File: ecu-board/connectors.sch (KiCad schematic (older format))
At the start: 39 parts, among them J10 Injector connector, J11 Cockpit connector, J12 EGO connector, J13 Chrankshaft Hall connector, J14 Camshaft Hall connector, J15 Ignition 1 connector, J16 Ignition 2 connector, J17 Camera connector, J18 Wheel Hall connector, J19 Speed sensor connector, J2 Battery power conenctor, J20 CAN connector, J21 12V connector, J22 PWRGND connector, J4 Motor connector, J5 Serial DB9 connector, J6 Controller connector, J7 Backlight connector, J8 IAT connector, J9 CLT connector

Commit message: Correct BOM to present components.
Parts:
- D10, D6, D7, D8, D9: Manufacturer (none) -> Generic; Part no. 3mm T-1 -> 0805
- D11: Manufacturer (none) -> ON Semi; Part no. (none) -> 1N5820G
- JP2, JP3, R10, R11, R5, R6, R7, R8, R9: Manufacturer (none) -> Generic; Part no. (none) -> 0805
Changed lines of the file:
@@
 F 1 "Ignition 1 connector" H 7330 3301 50  0000 L CNN
 F 2 "ecu-board-footprints:Terminal_Block_3x5.00mm" H 7250 3350 50  0001 C CNN
-F 3 "http://www.farnell.com/datasheets/2308387.pdf?_ga=2.20224184.1892952727.1549112209-881392492.1520553087" H 7250 3350 50  0001 C CNN
+F 3 "~" H 7250 3350 50  0001 C CNN
 F 4 "Würth" H 7250 3350 50  0001 C CNN "Manufacturer"
 F 5 "2141 Series" H 7250 3350 50  0001 C CNN "Part no."
@@
 F 1 "Ignition 2 connector" H 7330 4101 50  0000 L CNN
 F 2 "ecu-board-footprints:Terminal_Block_3x5.00mm" H 7250 4150 50  0001 C CNN
-F 3 "http://www.farnell.com/datasheets/2308387.pdf?_ga=2.20224184.1892952727.1549112209-881392492.1520553087" H 7250 4150 50  0001 C CNN
+F 3 "~" H 7250 4150 50  0001 C CNN
 F 4 "Würth" H 7250 4150 50  0001 C CNN "Manufacturer"
 F 5 "2141 Series" H 7250 4150 50  0001 C CNN "Part no."
@@
 F 2 "Resistors_SMD:R_0805_HandSoldering" V 9180 2000 50  0001 C CNN
 F 3 "~" H 9250 2000 50  0001 C CNN
+F 4 "Generic" H 9250 2000 50  0001 C CNN "Manufacturer"
+F 5 "0805" H 9250 2000 50  0001 C CNN "Part no."
 	1    9250 2000
 	1    0    0    -1
@@
 F 2 "Resistors_SMD:R_0805_HandSoldering" H 9250 3150 50  0001 C CNN
 F 3 "~" H 9250 3150 50  0001 C CNN
+F 4 "Generic" H 9250 3150 50  0001 C CNN "Manufacturer"
+F 5 "0805" H 9250 3150 50  0001 C CNN "Part no."
 	1    9250 3150
 	0    -1   -1   0
@@
 F 2 "Resistors_SMD:R_0805_HandSoldering" H 9250 4300 50  0001 C CNN
 F 3 "~" H 9250 4300 50  0001 C CNN
+F 4 "Generic" H 9250 4300 50  0001 C CNN "Manufacturer"
+F 5 "0805" H 9250 4300 50  0001 C CNN "Part no."
 	1    9250 4300
 	0    -1   -1   0
@@
 F 1 "LED" H 1442 2914 50  0000 C CNN
 F 2 "LEDs:LED_0805_HandSoldering" H 1450 2700 50  0001 C CNN
-F 3 "" H 1450 2700 50  0001 C CNN
-F 4 "3mm T-1" H 1450 2700 50  0001 C CNN "Part no."
+F 3 "~" H 1450 2700 50  0001 C CNN
+F 4 "0805" H 1450 2700 50  0001 C CNN "Part no."
+F 5 "Generic" H 1450 2700 50  0001 C CNN "Manufacturer"
 	1    1450 2700
 	-1   0    0    1
@@
 F 2 "LEDs:LED_0805_HandSoldering" H 1850 4450 50  0001 C CNN
 F 3 "~" H 1850 4450 50  0001 C CNN
-F 4 "3mm T-1" H 1850 4450 50  0001 C CNN "Part no."
+F 4 "0805" H 1850 4450 50  0001 C CNN "Part no."
+F 5 "Generic" H 1850 4450 50  0001 C CNN "Manufacturer"
 	1    1850 4450
 	-1   0    0    1
@@
 F 2 "LEDs:LED_0805_HandSoldering" H 7400 1500 50  0001 C CNN
 F 3 "~" H 7400 1500 50  0001 C CNN
-F 4 "3mm T-1" H 7400 1500 50  0001 C CNN "Part no."
+F 4 "0805" H 7400 1500 50  0001 C CNN "Part no."
+F 5 "Generic" H 7400 1500 50  0001 C CNN "Manufacturer"
 	1    7400 1500
 	-1   0    0    1
@@
 F 2 "LEDs:LED_0805_HandSoldering" H 2550 7600 50  0001 C CNN
 F 3 "~" H 2550 7600 50  0001 C CNN
-F 4 "3mm T-1" H 2550 7600 50  0001 C CNN "Part no."
+F 4 "0805" H 2550 7600 50  0001 C CNN "Part no."
+F 5 "Generic" H 2550 7600 50  0001 C CNN "Manufacturer"
 	1    2550 7600
 	-1   0    0    1
@@
 F 2 "Resistors_SMD:R_0805_HandSoldering" V 1030 2700 50  0001 C CNN
 F 3 "~" H 1100 2700 50  0001 C CNN
+F 4 "Generic" H 1100 2700 50  0001 C CNN "Manufacturer"
+F 5 "0805" H 1100 2700 50  0001 C CNN "Part no."
 	1    1100 2700
 	0    1    -1   0
@@
 F 2 "Resistors_SMD:R_0805_HandSoldering" V 1430 4450 50  0001 C CNN
 F 3 "~" H 1500 4450 50  0001 C CNN
+F 4 "Generic" H 1500 4450 50  0001 C CNN "Manufacturer"
+F 5 "0805" H 1500 4450 50  0001 C CNN "Part no."
 	1    1500 4450
 	0    1    1    0
@@
 F 2 "Resistors_SMD:R_0805_HandSoldering" V 6980 1500 50  0001 C CNN
 F 3 "~" H 7050 1500 50  0001 C CNN
+F 4 "Generic" H 7050 1500 50  0001 C CNN "Manufacturer"
+F 5 "0805" H 7050 1500 50  0001 C CNN "Part no."
 	1    7050 1500
 	0    1    1    0
@@
 F 2 "Resistors_SMD:R_0805_HandSoldering" V 2130 7600 50  0001 C CNN
 F 3 "~" H 2200 7600 50  0001 C CNN
+F 4 "Generic" H 2200 7600 50  0001 C CNN "Manufacturer"
+F 5 "0805" H 2200 7600 50  0001 C CNN "Part no."
 	1    2200 7600
 	0    1    1    0
@@
 F 1 "Camera connector" H 7330 5651 50  0000 L CNN
 F 2 "ecu-board-footprints:Terminal_Block_3x5.00mm" H 7250 5700 50  0001 C CNN
-F 3 "http://www.farnell.com/datasheets/2308387.pdf?_ga=2.20224184.1892952727.1549112209-881392492.1520553087" H 7250 5700 50  0001 C CNN
+F 3 "~" H 7250 5700 50  0001 C CNN
 F 4 "Würth" H 7250 5700 50  0001 C CNN "Manufacturer"
 F 5 "2141 Series" H 7250 5700 50  0001 C CNN "Part no."
@@
 F 2 "LEDs:LED_0805_HandSoldering" H 1800 5950 50  0001 C CNN
 F 3 "~" H 1800 5950 50  0001 C CNN
-F 4 "3mm T-1" H 1800 5950 50  0001 C CNN "Part no."
+F 4 "0805" H 1800 5950 50  0001 C CNN "Part no."
+F 5 "Generic" H 1800 5950 50  0001 C CNN "Manufacturer"
 	1    1800 5950
 	-1   0    0    1
@@
 F 2 "Resistors_SMD:R_0805_HandSoldering" V 1380 5950 50  0001 C CNN
 F 3 "~" H 1450 5950 50  0001 C CNN
+F 4 "Generic" H 1450 5950 50  0001 C CNN "Manufacturer"
+F 5 "0805" H 1450 5950 50  0001 C CNN "Part no."
 	1    1450 5950
 	0    1    1    0
@@
 F 1 "Serial DB9 connector" H 5029 1855 50  0000 L CNN
 F 2 "ecu-board-footprints:TE_5747844-4" H 4850 1900 50  0001 C CNN
-F 3 "" H 4850 1900 50  0001 C CNN
+F 3 "~" H 4850 1900 50  0001 C CNN
 F 4 "TE Connectivity" H 4850 1900 50  0001 C CNN "Manufacturer"
 F 5 "5747844-4" H 5250 1750 50  0000 C CNN "Part no."
@@
 F 2 "Diodes_THT:D_A-405_P10.16mm_Horizontal" H 1700 2500 50  0001 C CNN
 F 3 "~" H 1700 2500 50  0001 C CNN
+F 4 "ON Semi" H 1700 2500 50  0001 C CNN "Manufacturer"
+F 5 "1N5820G" H 1700 2500 50  0001 C CNN "Part no."
 	1    1700 2500
 	0    -1   1    0
@@
 F 2 "Resistors_SMD:R_0805_HandSoldering" V 4530 7650 50  0001 C CNN
 F 3 "~" H 4600 7650 50  0001 C CNN
+F 4 "Generic" H 4600 7650 50  0001 C CNN "Manufacturer"
+F 5 "0805" H 4600 7650 50  0001 C CNN "Part no."
 	1    4600 7650
 	0    1    1    0

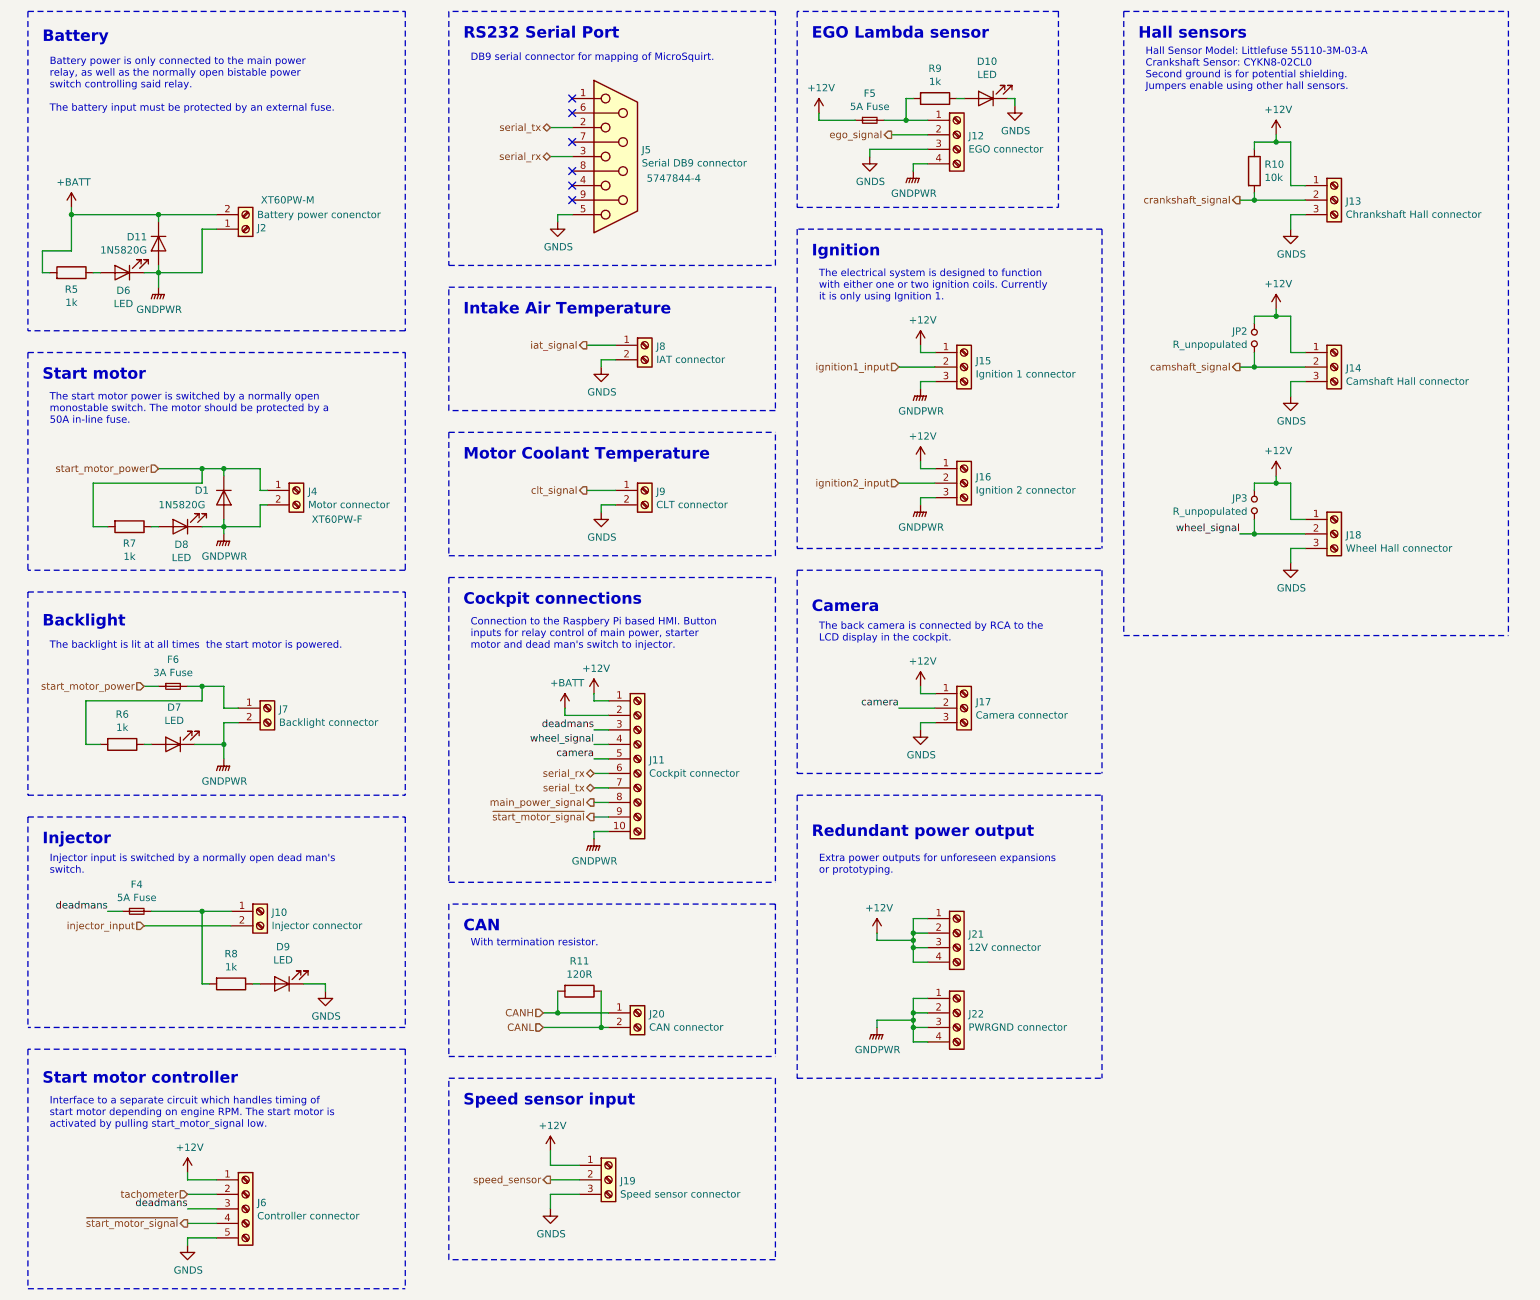
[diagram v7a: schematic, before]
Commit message: Split MicroSquirt breakout connector into three separate connectors. Old connector was impossible to route.
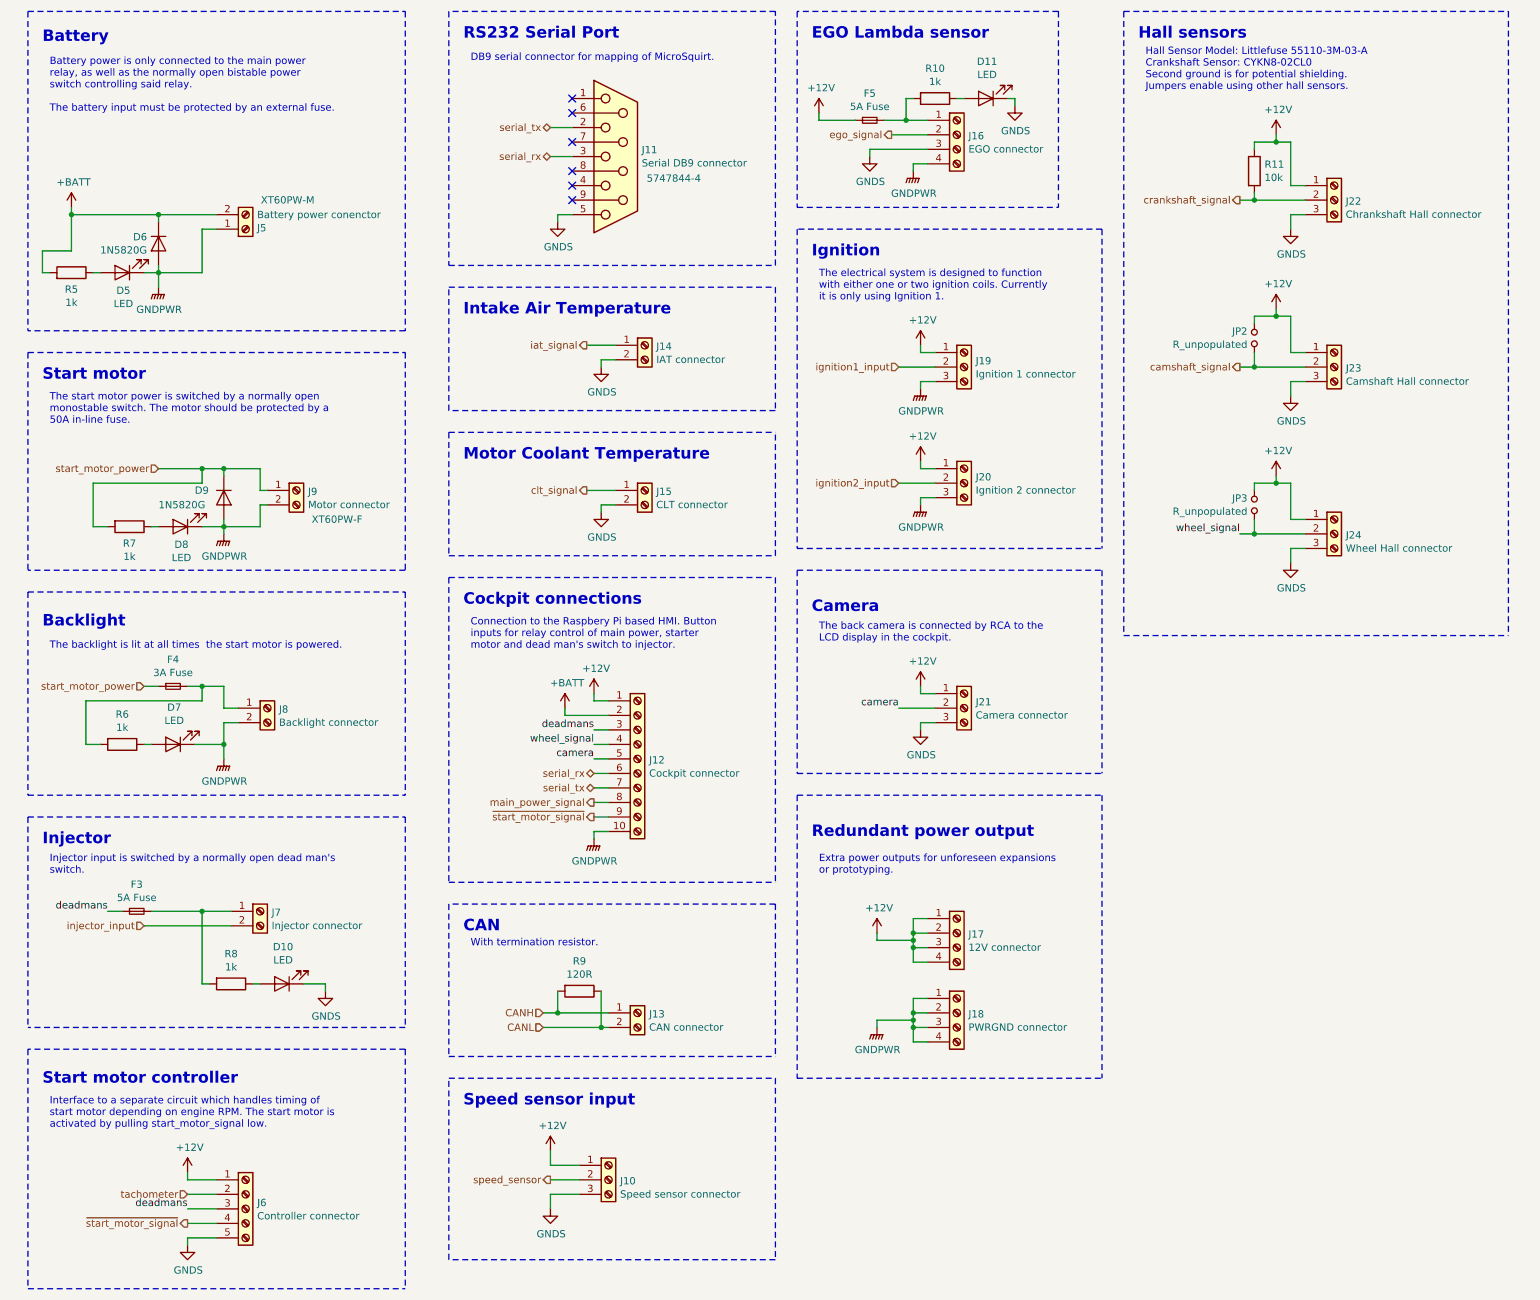
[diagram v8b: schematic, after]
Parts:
- renumbered D9 to D10, D10 to D11, D6 to D5, D11 to D6, D1 to D9, F4 to F3, F6 to F4, J19 to J10, J5 to J11, J11 to J12, J20 to J13, J8 to J14, J9 to J15, J12 to J16, J21 to J17, J22 to J18, J15 to J19, J16 to J20, J17 to J21, J13 to J22, J14 to J23, J18 to J24, J2 to J5, J10 to J7, J7 to J8, J4 to J9, R9 to R10, R10 to R11, R11 to R9
